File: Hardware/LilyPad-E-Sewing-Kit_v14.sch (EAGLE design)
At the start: 42 parts

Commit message: Updated schematic and board files --missing connection fixed
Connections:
- removed net N$3: S3.O, SLIDEOFF.1
- net SWITCH: now also S3.O, SLIDEOFF.1
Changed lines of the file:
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@@
 <wire x1="60.96" y1="55.88" x2="60.96" y2="53.34" width="0.1524" layer="91"/>
+</segment>
+<segment>
+<pinref part="S3" gate="1" pin="O"/>
+<pinref part="SLIDEOFF" gate="G$1" pin="1"/>
+<wire x1="162.56" y1="104.14" x2="154.94" y2="104.14" width="0.1524" layer="91"/>
 </segment>
 </net>
@@
 </segment>
 </net>
-<net name="N$3" class="0">
-<segment>
-<pinref part="S3" gate="1" pin="O"/>
-<pinref part="SLIDEOFF" gate="G$1" pin="1"/>
-<wire x1="162.56" y1="104.14" x2="154.94" y2="104.14" width="0.1524" layer="91"/>
-</segment>
-</net>

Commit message: Updated Board and Schematic files
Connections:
- new net ON: S3.S, SLIDEON.1
- net N$2: no longer S3.P, SLIDEON.1
- net SWITCH: now also S3.P; no longer S3.O
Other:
- moved on the sheet: S3
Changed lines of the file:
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@@
 <instance part="S1" gate="1" x="43.18" y="137.16"/>
 <instance part="S2" gate="G$1" x="170.18" y="124.46"/>
-<instance part="S3" gate="1" x="167.64" y="106.68" rot="R180"/>
+<instance part="S3" gate="1" x="167.64" y="106.68"/>
 <instance part="FRAME1" gate="G$1" x="0" y="0"/>
 <instance part="FRAME1" gate="V" x="147.32" y="0"/>
@@
 <pinref part="P+3" gate="G$1" pin="VCC"/>
 <wire x1="220.98" y1="104.14" x2="220.98" y2="109.22" width="0.1524" layer="91"/>
-</segment>
-<segment>
-<pinref part="SLIDEON" gate="G$1" pin="1"/>
-<wire x1="185.42" y1="106.68" x2="170.18" y2="106.68" width="0.1524" layer="91"/>
-<pinref part="S3" gate="1" pin="P"/>
 </segment>
 </net>
@@
 </segment>
 <segment>
-<pinref part="S3" gate="1" pin="O"/>
 <pinref part="SLIDEOFF" gate="G$1" pin="1"/>
-<wire x1="162.56" y1="104.14" x2="154.94" y2="104.14" width="0.1524" layer="91"/>
+<wire x1="154.94" y1="104.14" x2="162.56" y2="104.14" width="0.1524" layer="91"/>
+<wire x1="162.56" y1="104.14" x2="162.56" y2="106.68" width="0.1524" layer="91"/>
+<pinref part="S3" gate="1" pin="P"/>
+<wire x1="162.56" y1="106.68" x2="165.1" y2="106.68" width="0.1524" layer="91"/>
 </segment>
 </net>
@@
 </segment>
 </net>
+<net name="ON" class="0">
+<segment>
+<pinref part="S3" gate="1" pin="S"/>
+<wire x1="172.72" y1="104.14" x2="180.34" y2="104.14" width="0.1524" layer="91"/>
+<wire x1="180.34" y1="104.14" x2="180.34" y2="106.68" width="0.1524" layer="91"/>
+<pinref part="SLIDEON" gate="G$1" pin="1"/>
+<wire x1="180.34" y1="106.68" x2="185.42" y2="106.68" width="0.1524" layer="91"/>
+</segment>
+</net>

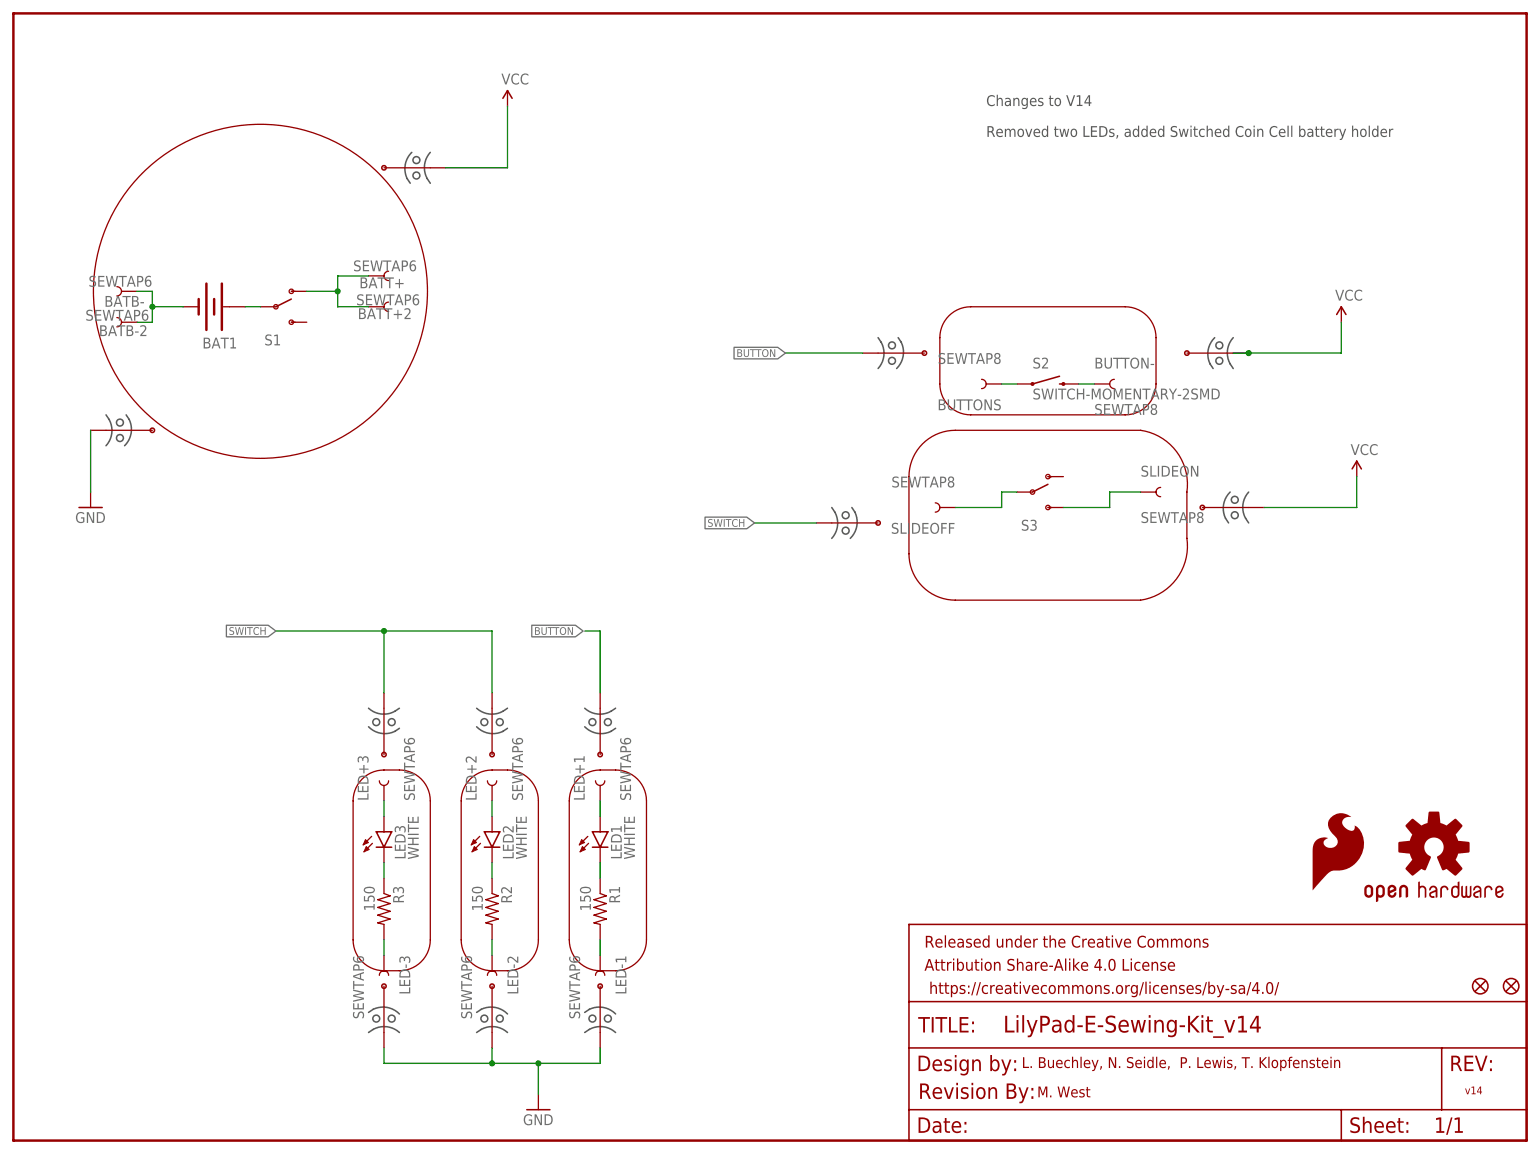
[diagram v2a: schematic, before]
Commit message: Updated brd and sch files per engineering design review 6/13/16
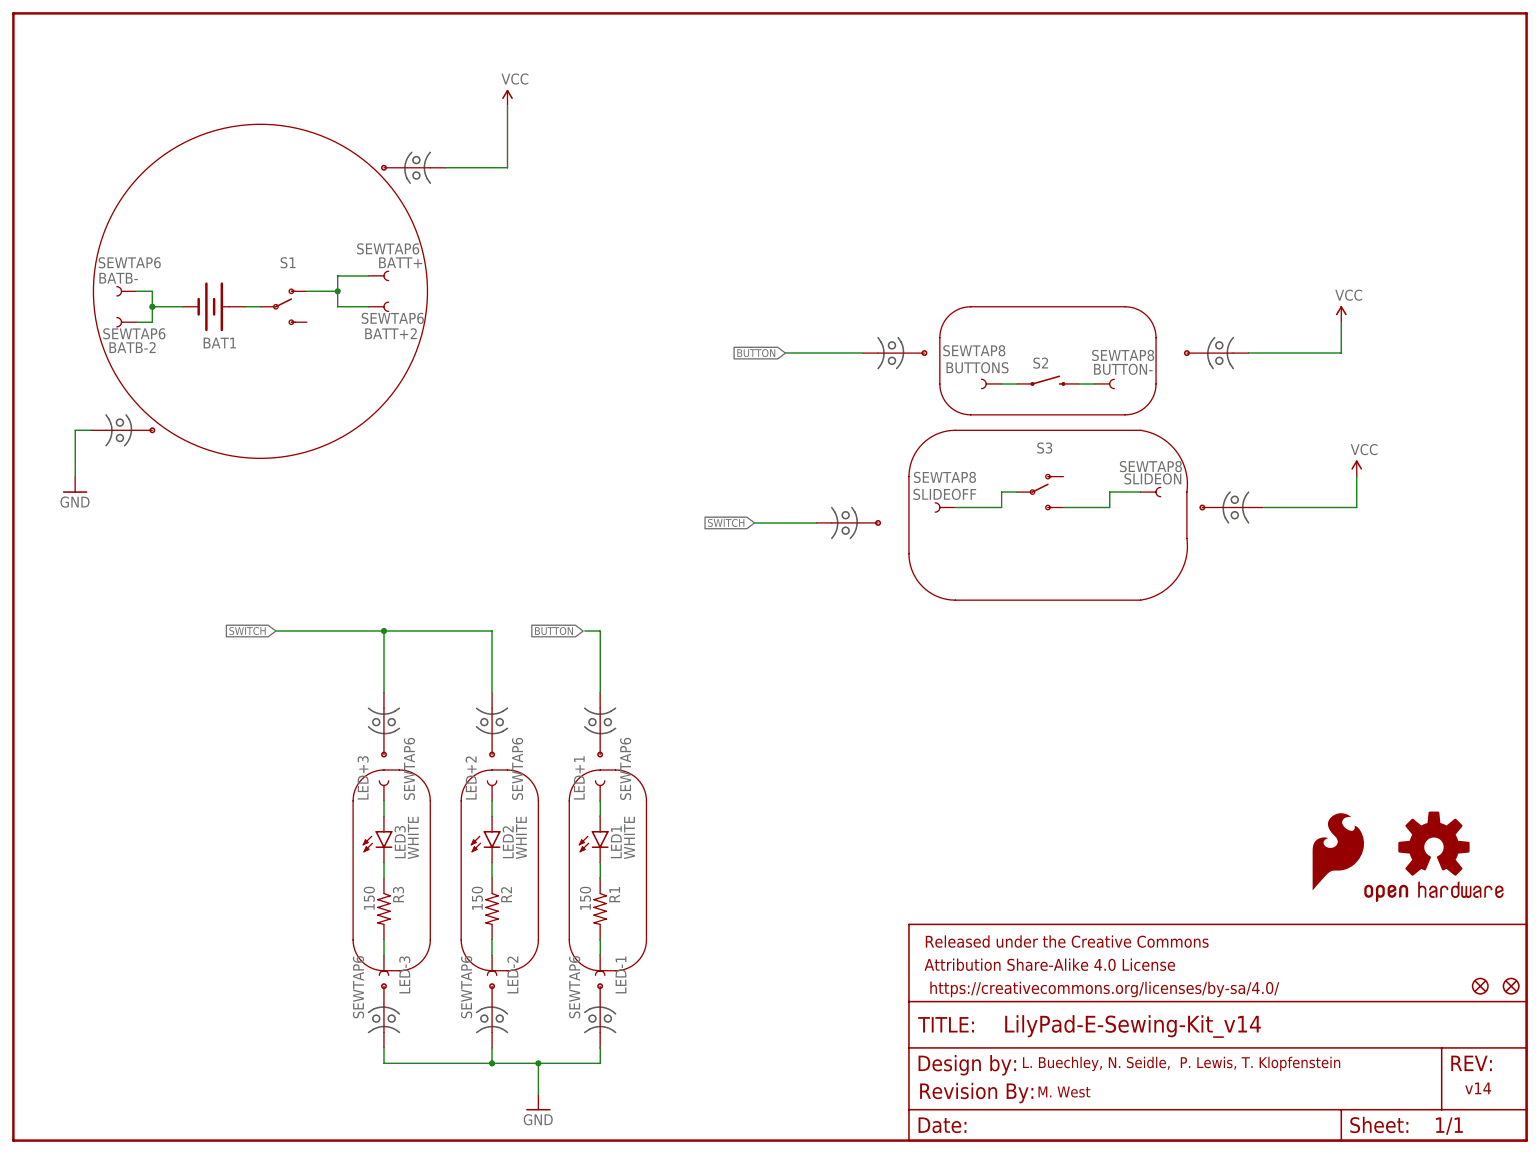
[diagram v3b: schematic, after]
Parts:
- S1: value (none) -> S1
- S3: value (none) -> S3
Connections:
- removed net N$2: BATT+.1, BATT+2.1, BUTTON-.1, MB+.P$1, MB1.P$1, MB2.P$1, S1.O, S2.2
- removed net ON: S3.S, SLIDEON.1
- new net VCC: BATT+.1, BATT+2.1, BUTTON-.1, MB+.P$1, MB1.P$1, MB2.P$1, S1.O, S2.2, S3.S, SLIDEON.1
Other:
- note removed: "Changes to V14"
- note removed: "Removed two LEDs, added Switched Coin Cell battery holder"
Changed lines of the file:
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@@
 <part name="MB5" library="Testing" deviceset="MOUSE-BITE-1" device="2_HOLES"/>
 <part name="MB6" library="Testing" deviceset="MOUSE-BITE-1" device="2_HOLES"/>
-<part name="S1" library="SparkFun-Electromechanical" deviceset="SWITCH-SPDT" device="SMD"/>
+<part name="S1" library="SparkFun-Electromechanical" deviceset="SWITCH-SPDT" device="SMD" value="S1"/>
 <part name="S2" library="SparkFun-Electromechanical" deviceset="SWITCH-MOMENTARY-2" device="SMD"/>
-<part name="S3" library="SparkFun-Electromechanical" deviceset="SWITCH-SPDT" device="SMD"/>
+<part name="S3" library="SparkFun-Electromechanical" deviceset="SWITCH-SPDT" device="SMD" value="S3"/>
 <part name="FRAME1" library="SparkFun-Aesthetics" deviceset="FRAME-LETTER" device=""/>
 <part name="U$1" library="SparkFun-Aesthetics" deviceset="REVISION" device=""/>
@@
 <wire x1="91.44" y1="33.02" x2="91.44" y2="55.88" width="0.2032" layer="94"/>
 <circle x="40.64" y="139.7" radius="27.4743" width="0.2032" layer="94"/>
-<text x="160.02" y="170.18" size="1.778" layer="97">Changes to V14</text>
-<text x="160.02" y="165.1" size="1.778" layer="97">Removed two LEDs, added Switched Coin Cell battery holder</text>
 <wire x1="55.88" y1="55.88" x2="60.96" y2="60.96" width="0.2032" layer="94" curve="-90"/>
 <wire x1="60.96" y1="60.96" x2="63.5" y2="60.96" width="0.2032" layer="94"/>
@@
 <text x="165.862" y="11.938" size="1.778" layer="94">L. Buechley, N. Seidle,  P. Lewis, T. Klopfenstein</text>
 <text x="168.402" y="7.112" size="1.778" layer="94">M. West</text>
-<text x="238.76" y="7.62" size="1.27" layer="94">v14</text>
+<text x="238.76" y="7.62" size="1.9304" layer="94">v14</text>
 </plain>
 <instances>
-<instance part="SLIDEOFF" gate="G$1" x="152.4" y="104.14" rot="R180"/>
+<instance part="SLIDEOFF" gate="G$1" x="152.4" y="104.14" smashed="yes" rot="R180">
+<attribute name="NAME" x="158.496" y="107.188" size="1.778" layer="95" rot="R180"/>
+<attribute name="VALUE" x="158.496" y="109.982" size="1.778" layer="96" rot="R180"/>
+</instance>
 <instance part="SLIDEON" gate="G$1" x="187.96" y="106.68" smashed="yes">
-<attribute name="NAME" x="185.42" y="109.22" size="1.778" layer="95"/>
-<attribute name="VALUE" x="185.42" y="101.6" size="1.778" layer="96"/>
+<attribute name="NAME" x="182.626" y="107.95" size="1.778" layer="95"/>
+<attribute name="VALUE" x="181.864" y="109.982" size="1.778" layer="96"/>
 </instance>
 <instance part="BUTTONS" gate="G$1" x="160.02" y="124.46" smashed="yes" rot="R180">
-<attribute name="NAME" x="162.56" y="121.92" size="1.778" layer="95" rot="R180"/>
-<attribute name="VALUE" x="162.56" y="129.54" size="1.778" layer="96" rot="R180"/>
+<attribute name="NAME" x="163.83" y="128.016" size="1.778" layer="95" rot="R180"/>
+<attribute name="VALUE" x="163.322" y="130.81" size="1.778" layer="96" rot="R180"/>
 </instance>
 <instance part="BUTTON-" gate="G$1" x="180.34" y="124.46" smashed="yes">
-<attribute name="NAME" x="177.8" y="127" size="1.778" layer="95"/>
-<attribute name="VALUE" x="177.8" y="119.38" size="1.778" layer="96"/>
+<attribute name="NAME" x="177.546" y="125.984" size="1.778" layer="95"/>
+<attribute name="VALUE" x="177.292" y="128.27" size="1.778" layer="96"/>
 </instance>
 <instance part="R2" gate="G$1" x="78.74" y="38.1" rot="R270"/>
@@
 </instance>
 <instance part="BATB-2" gate="G$1" x="17.78" y="134.62" smashed="yes" rot="R180">
-<attribute name="NAME" x="22.098" y="134.112" size="1.778" layer="95" rot="R180"/>
-<attribute name="VALUE" x="22.352" y="136.652" size="1.778" layer="96" rot="R180"/>
+<attribute name="NAME" x="23.622" y="131.318" size="1.778" layer="95" rot="R180"/>
+<attribute name="VALUE" x="25.146" y="133.604" size="1.778" layer="96" rot="R180"/>
 </instance>
 <instance part="BATT+2" gate="G$1" x="60.96" y="137.16" smashed="yes">
-<attribute name="NAME" x="56.642" y="135.128" size="1.778" layer="95"/>
-<attribute name="VALUE" x="56.388" y="137.414" size="1.778" layer="96"/>
+<attribute name="NAME" x="57.658" y="131.826" size="1.778" layer="95"/>
+<attribute name="VALUE" x="57.15" y="134.366" size="1.778" layer="96"/>
 </instance>
 <instance part="BATB-" gate="G$1" x="17.78" y="139.7" smashed="yes" rot="R180">
-<attribute name="NAME" x="21.59" y="138.938" size="1.778" layer="95" rot="R180"/>
-<attribute name="VALUE" x="22.86" y="142.24" size="1.778" layer="96" rot="R180"/>
+<attribute name="NAME" x="20.574" y="142.748" size="1.778" layer="95" rot="R180"/>
+<attribute name="VALUE" x="24.384" y="145.288" size="1.778" layer="96" rot="R180"/>
 </instance>
 <instance part="BATT+" gate="G$1" x="60.96" y="142.24" smashed="yes">
-<attribute name="NAME" x="56.896" y="140.208" size="1.778" layer="95"/>
-<attribute name="VALUE" x="55.88" y="143.002" size="1.778" layer="96"/>
+<attribute name="NAME" x="59.944" y="143.51" size="1.778" layer="95"/>
+<attribute name="VALUE" x="56.388" y="145.796" size="1.778" layer="96"/>
 </instance>
 <instance part="MB+" gate="G$1" x="68.58" y="160.02" rot="R180"/>
 <instance part="MB-" gate="G$1" x="15.24" y="116.84"/>
-<instance part="GND1" gate="1" x="12.7" y="104.14"/>
+<instance part="GND1" gate="1" x="10.16" y="106.68"/>
 <instance part="P+1" gate="G$1" x="81.28" y="170.18"/>
 <instance part="P+2" gate="G$1" x="218.44" y="134.62"/>
@@
 <instance part="MB5" gate="G$1" x="60.96" y="71.12" rot="R270"/>
 <instance part="MB6" gate="G$1" x="60.96" y="17.78" rot="R90"/>
-<instance part="S1" gate="1" x="43.18" y="137.16"/>
-<instance part="S2" gate="G$1" x="170.18" y="124.46"/>
-<instance part="S3" gate="1" x="167.64" y="106.68"/>
+<instance part="S1" gate="1" x="43.18" y="137.16" smashed="yes">
+<attribute name="NAME" x="43.815" y="143.51" size="1.778" layer="95"/>
+</instance>
+<instance part="S2" gate="G$1" x="170.18" y="124.46" smashed="yes">
+<attribute name="NAME" x="167.64" y="127" size="1.778" layer="95"/>
+</instance>
+<instance part="S3" gate="1" x="167.64" y="106.68" smashed="yes">
+<attribute name="NAME" x="168.275" y="113.03" size="1.778" layer="95"/>
+</instance>
 <instance part="FRAME1" gate="G$1" x="0" y="0"/>
 <instance part="FRAME1" gate="V" x="147.32" y="0"/>
@@
 </segment>
 </net>
-<net name="N$2" class="0">
+<net name="VCC" class="0">
 <segment>
 <pinref part="S1" gate="1" pin="O"/>
@@
 <pinref part="P+2" gate="G$1" pin="VCC"/>
 <wire x1="218.44" y1="134.62" x2="218.44" y2="129.54" width="0.1524" layer="91"/>
-<wire x1="218.44" y1="129.54" x2="203.2" y2="129.54" width="0.1524" layer="91"/>
 <pinref part="MB2" gate="G$1" pin="P$1"/>
-<wire x1="203.2" y1="129.54" x2="200.66" y2="129.54" width="0.1524" layer="91"/>
-<junction x="203.2" y="129.54"/>
+<wire x1="203.2" y1="129.54" x2="218.44" y2="129.54" width="0.1524" layer="91"/>
 </segment>
 <segment>
@@
 <wire x1="220.98" y1="104.14" x2="220.98" y2="109.22" width="0.1524" layer="91"/>
 </segment>
+<segment>
+<pinref part="S3" gate="1" pin="S"/>
+<wire x1="172.72" y1="104.14" x2="180.34" y2="104.14" width="0.1524" layer="91"/>
+<wire x1="180.34" y1="104.14" x2="180.34" y2="106.68" width="0.1524" layer="91"/>
+<pinref part="SLIDEON" gate="G$1" pin="1"/>
+<wire x1="180.34" y1="106.68" x2="185.42" y2="106.68" width="0.1524" layer="91"/>
+</segment>
 </net>
 <net name="GND" class="0">
-<segment>
-<pinref part="MB-" gate="G$1" pin="P$1"/>
-<pinref part="GND1" gate="1" pin="GND"/>
-<wire x1="12.7" y1="116.84" x2="12.7" y2="106.68" width="0.1524" layer="91"/>
-</segment>
 <segment>
 <pinref part="BATB-" gate="G$1" pin="1"/>
@@
 <junction x="86.36" y="12.7"/>
 </segment>
+<segment>
+<pinref part="MB-" gate="G$1" pin="P$1"/>
+<wire x1="12.7" y1="116.84" x2="10.16" y2="116.84" width="0.1524" layer="91"/>
+<wire x1="10.16" y1="116.84" x2="10.16" y2="109.22" width="0.1524" layer="91"/>
+<pinref part="GND1" gate="1" pin="GND"/>
+</segment>
 </net>
 <net name="BUTTON" class="0">
@@
 </segment>
 </net>
-<net name="ON" class="0">
-<segment>
-<pinref part="S3" gate="1" pin="S"/>
-<wire x1="172.72" y1="104.14" x2="180.34" y2="104.14" width="0.1524" layer="91"/>
-<wire x1="180.34" y1="104.14" x2="180.34" y2="106.68" width="0.1524" layer="91"/>
-<pinref part="SLIDEON" gate="G$1" pin="1"/>
-<wire x1="180.34" y1="106.68" x2="185.42" y2="106.68" width="0.1524" layer="91"/>
-</segment>
-</net>

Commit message: Silk update for consistency amongst the Lilypad product line.
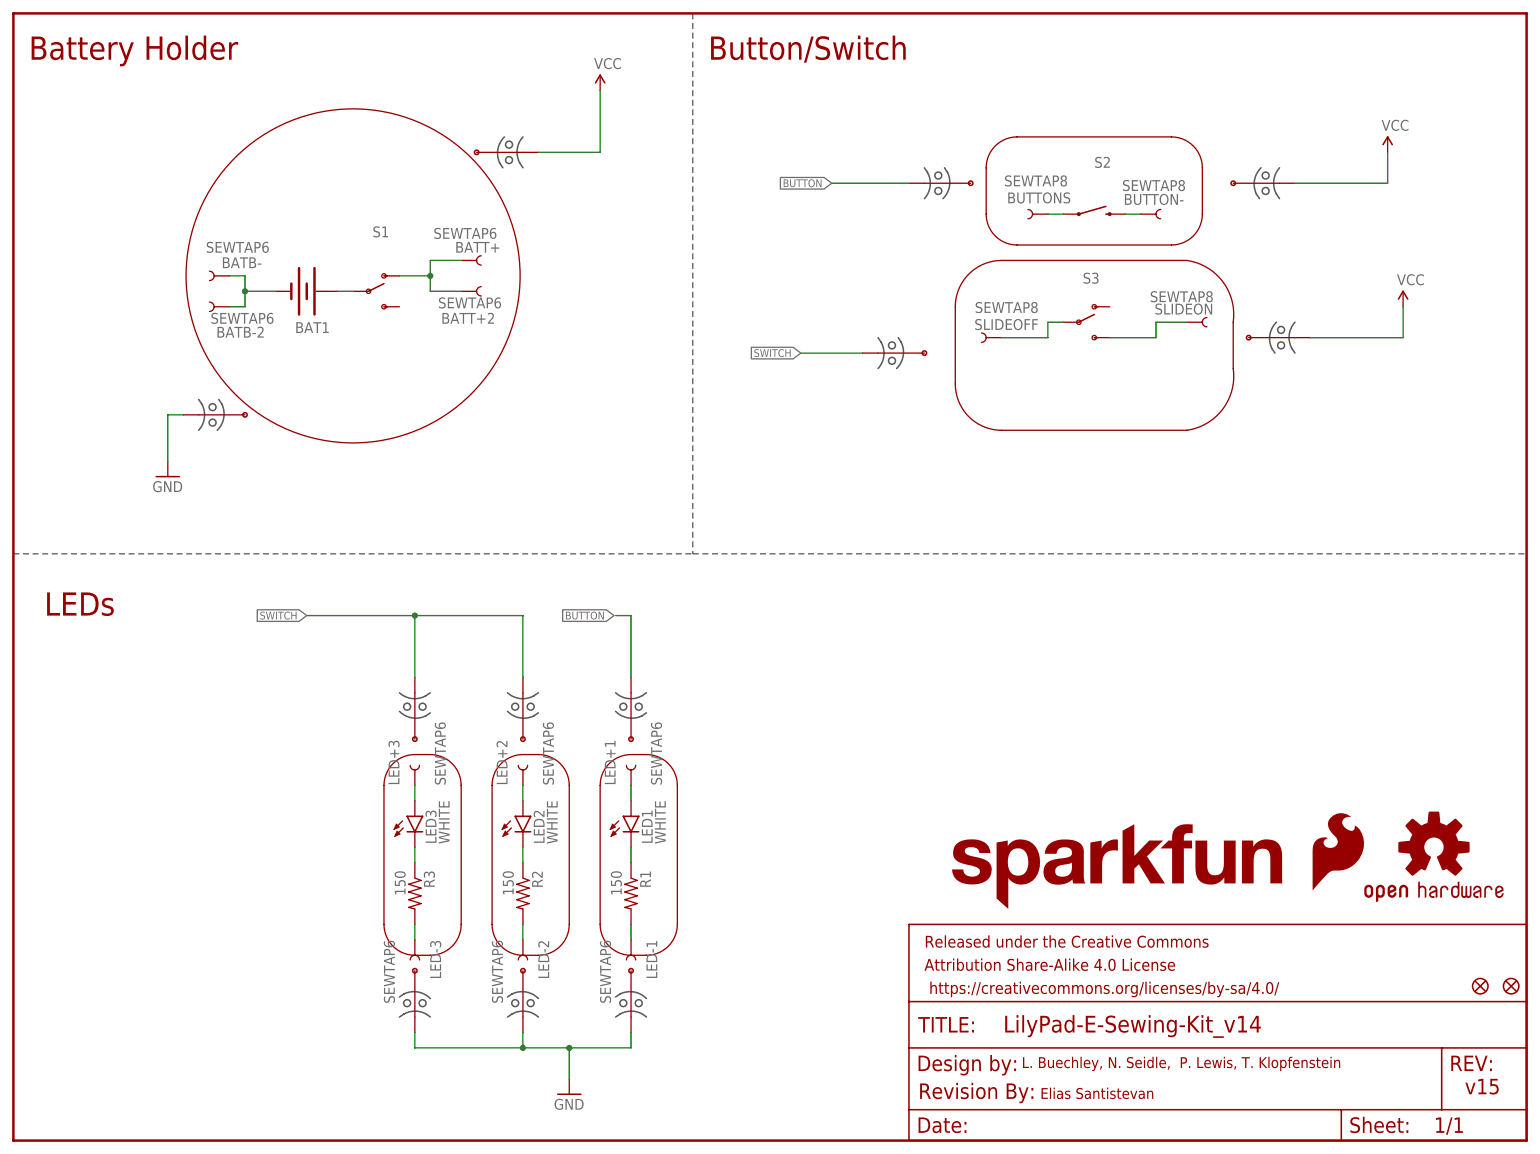
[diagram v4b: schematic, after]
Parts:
- added LOGO3: SFE_LOGO_NAME.1_INCH, SparkFun-Aesthetics:SFE_LOGO_NAME.1_INCH
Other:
- note added: "Battery Holder"
- note added: "Button/Switch"
- note added: "Elias Santistevan"
- note added: "LEDs"
- note added: "v15"
- note removed: "M. West"
- note removed: "v14"
- moved on the sheet: BAT1, BATB-, BATB-2, BATT+, BATT+2, BUTTON-, BUTTONS, LED+1, LED+2, LED+3, LED-1, LED-2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
